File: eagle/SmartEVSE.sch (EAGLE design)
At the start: 44 parts, among them IC1 78L05SMD, IC2 LM7332MA, IC3 MCP9701A, K2 AQH1213AJ, Q1 16Mhz, U1 PIC18F25K22-I/SO, U2 SN65HVD3082ED, X1 MKDSN1,5/9-5,08, X2 AST027-06

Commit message: Second commit of Smart EVSE
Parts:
- removed JP1: (no value), jumper:JP1Q
- removed LED: (no value), pinhead:PINHD-1X2
- removed U1: PIC18F25K22-I/SO, pic_18f25k22:PIC18F25K22-I/SO
- added C13: 100n, rcl:C-EUC0805
- added C14: 10000u 16V, rcl:CPOL-EUE10-22.5
- added D1, D4: BAT54S, diode:BAT54S
- added IC4: PIC18F25K22-I/SOSSOP, pic_18f25k22:PIC18F25K22-I/SOSSOP
- added IC6: TC4424A, tc4424:TC4424AVOA
- added R14: 100R, resistor:R-EU_R0805
- added R15: 10K, resistor:R-EU_R0805
- added R16: 5K1, resistor:R-EU_R0805
- C1, C2: value 22p -> 18p
- C3: value 100n -> 10u 16v; device rcl:C-EUC0805 -> rcl:C-EUC1206
- C7: value 10u -> 10u 16v; device rcl:CPOL-EUE5-5 -> rcl:C-EUC1206
- C9: value 100u -> n.c.; device rcl:CPOL-EUE5-5 -> rcl:CPOL-EUSMCC
- F2: device ptc-littlefuse:1206L -> ptc-littlefuse:1206L"
- IC1: value 78L05SMD -> LP2985IM5-5.0; device linear:78L05SMD -> v-reg-micrel:MIC5219XX
- K1: value AQH1213AJ -> AQH1213AX
- Q1: value 16Mhz -> CTS_32X25_SMD; device special:XTAL/S -> cts_crystal:CTS_32X25_SMD
- R1: value 120R -> 10K
- R10: value 168R -> 169R
- R12: value 1K -> 1K 1%
- R13: value 330R -> 10K
- R3, R4: value 27K -> 15K
- renumbered K2 to K1, U2 to IC5
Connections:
- removed net N$2: JP1.2, R1.1
- removed net N$30: F2.2, X1-6.KL
- removed net N$4: IC5.A, R1.2, X1-4.KL
- new net N$17: C13.1, C14.+, D1.C2, D4.C2, IC6.VDD, R14.2
- new net N$18: IC4.RA5, IC6.IN_A, R15.1
- new net N$32: F2.2, X1-3.KL
- new net N$33: R1.2, X1-5.KL
- new net RS485_A: IC5.A, X1-1.KL
- new net RS485_B: IC5.B, X1-2.KL
- net +12V: now also C7.1, IC1.EN, IC1.IN, R14.1; no longer C7.+, IC1G$1.VIN
- net GND: now also C13.2, C14.-, C7.2, D1.A1, D4.A1, IC1.GND, IC4.VSS, IC4.VSS_2, IC6.GND, Q1.GND, R13.2, R15.2, R16.1, X1-4.KL; no longer C7.-, IC1G$1.GND@1, IC1G$1.GND@2, IC1G$1.GND@3, IC1G$1.GND@4, U1.VSS, U1.VSS_2, X1-3.KL, X1-7.KL
- net LCD0: now also IC4.RB0; no longer U1.RB0
- net LCD1: now also IC4.RB1; no longer U1.RB1
- net LCD2: now also IC4.RB2; no longer U1.RB2
- net LCD3: now also IC4.RB3; no longer U1.RB3
- net LCD4: now also IC4.RC0; no longer U1.RC0
- net LCD6: now also IC4.RC3; no longer U1.RC3
- net LCD7: now also IC4.RC4; no longer U1.RC4
- net LCD8: now also IC4.RC5; no longer U1.RC5
- net N$1: now also IC4.RC1, R1.1, R16.2; no longer IC5.B, JP1.1, X1-5.KL
- net N$11: now also IC4.RC2; no longer U1.RC2
- net N$13: now also IC4.RA0; no longer U1.RA0
- net N$16: now also IC4.RA1; no longer U1.RA1
- net N$20: now also IC4.RB4; no longer U1.RB4
- net N$25: now also IC4.RB5; no longer U1.RB5
- net N$27: now also D1.C1A2, IC6.OUT_A, X1-6.KL; no longer LED.2, U1.RA5, X1-1.KL
- net N$28: now also IC4.MCLR*; no longer U1.MCLR*
- net N$29: now also D4.C1A2, IC6.OUT_B, X1-7.KL; no longer LED.1, R13.1, X1-2.KL
- net N$3: now also IC4.RA4, IC6.IN_B, R13.1; no longer R13.2, U1.RA4
- net N$31: now also IC4.RA2; no longer U1.RA2
- net N$34: now also IC4.RB7; no longer U1.RB7
- net N$35: now also IC4.RB6; no longer U1.RB6
- net N$5: now also IC4.RC6; no longer U1.RC6
- net N$6: now also IC4.RC7; no longer U1.RC7
- net N$7: now also IC4.RA7, Q1.X1; no longer Q1.2, U1.RA7
- net N$8: now also IC4.RA6, Q1.X2; no longer Q1.1, U1.RA6
- net VCC: now also IC1.OUT, IC4.VDD; no longer IC1G$1.VOUT, U1.VDD
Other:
- note added: "Actuator Driver"
- note added: "Smart EVSE rev 1.3b"
- note added: "Solenoid"
- note added: "Solid State Relay"
- note added: "Temperature sensor"
- note added: "lock_state"
- note removed: "LED"
- moved on the sheet: C2, R1, R12, R13, X1-1, X1-2, X1-3, X1-4, X1-5

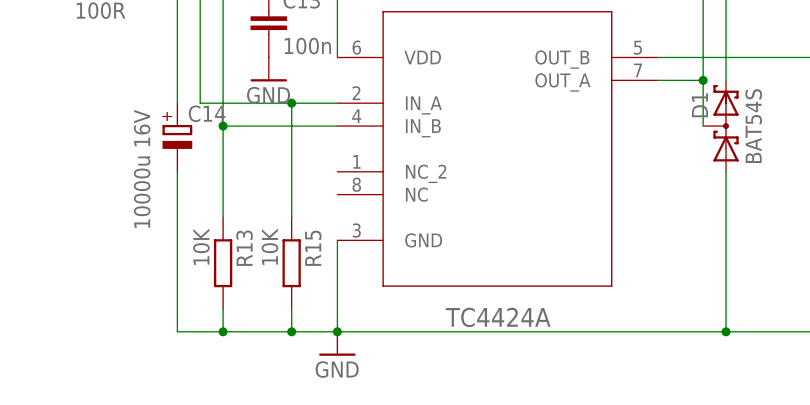
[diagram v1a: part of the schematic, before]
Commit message: version 1.05, LCD menu added
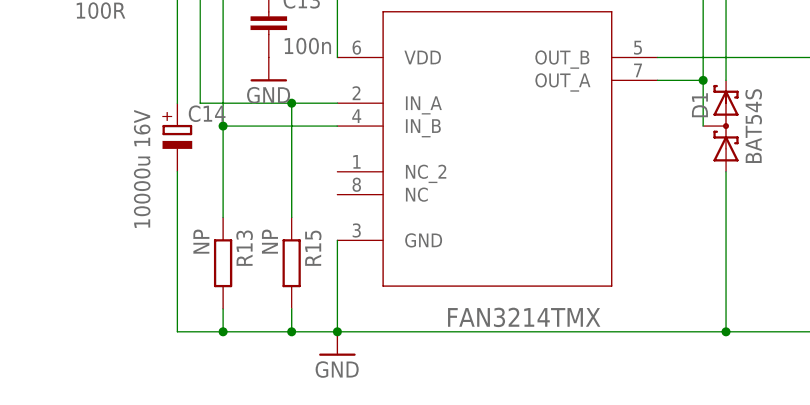
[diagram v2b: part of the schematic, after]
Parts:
- IC6: value TC4424A -> FAN3214TMX
- R13, R15: value 10K -> NP
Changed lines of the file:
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@@
 <?xml version="1.0" encoding="utf-8"?>
 <!DOCTYPE eagle SYSTEM "eagle.dtd">
-<eagle version="6.2">
+<eagle version="6.6.0">
 <drawing>
 <settings>
@@
 <part name="D1" library="diode" deviceset="BAT54S" device=""/>
 <part name="D4" library="diode" deviceset="BAT54S" device=""/>
-<part name="IC6" library="tc4424" deviceset="TC4424AVOA" device="" value="TC4424A"/>
+<part name="IC6" library="tc4424" deviceset="TC4424AVOA" device="" value="FAN3214TMX"/>
 <part name="GND11" library="supply1" deviceset="GND" device=""/>
 <part name="C13" library="rcl" deviceset="C-EU" device="C0805" value="100n"/>
 <part name="GND12" library="supply1" deviceset="GND" device=""/>
-<part name="R13" library="resistor" deviceset="R-EU_" device="R0805" value="10K"/>
-<part name="R15" library="resistor" deviceset="R-EU_" device="R0805" value="10K"/>
+<part name="R13" library="resistor" deviceset="R-EU_" device="R0805" value="NP"/>
+<part name="R15" library="resistor" deviceset="R-EU_" device="R0805" value="NP"/>
 <part name="C14" library="rcl" deviceset="CPOL-EU" device="E10-22.5" value="10000u 16V"/>
 <part name="C7" library="rcl" deviceset="C-EU" device="C1206" value="10u 16v"/>
